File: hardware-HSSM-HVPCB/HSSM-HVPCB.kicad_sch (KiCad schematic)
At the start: 22 parts, among them J1 2086-1103, J2 2601-1110, K1 G6DN-1A-L DC12, K2 G6DN-1A-L DC12, U1 LNK3202D-TL, U2 CS5480-INZ

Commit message: [#3] SCH LNK3204 connections correct output capacitor connection
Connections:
- net +12V: now also C3.1
- net at C1.2, C4.1, D1.1 (K)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: no longer C3.1
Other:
- moved on the sheet: C3, R4
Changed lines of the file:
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@@
 	(paper "A4")
+	(junction
+		(at 240.03 105.41)
+		(diameter 0)
+		(color 0 0 0 0)
+	)
 	(junction
 		(at 224.79 86.36)
@@
 	)
 	(junction
+		(at 251.46 86.36)
+		(diameter 0)
+		(color 0 0 0 0)
+	)
+	(junction
 		(at 240.03 71.12)
 		(diameter 0)
@@
 	)
 	(junction
-		(at 224.79 105.41)
+		(at 160.02 93.98)
 		(diameter 0)
 		(color 0 0 0 0)
 	)
 	(junction
-		(at 240.03 105.41)
-		(diameter 0)
-		(color 0 0 0 0)
-	)
-	(junction
-		(at 160.02 93.98)
+		(at 251.46 105.41)
 		(diameter 0)
 		(color 0 0 0 0)
@@
 	(wire
 		(pts
-			(xy 204.47 105.41) (xy 224.79 105.41)
-		)
-		(stroke
-			(width 0)
-			(type default)
-		)
-	)
-	(wire
-		(pts
-			(xy 240.03 97.79) (xy 240.03 105.41)
+			(xy 204.47 105.41) (xy 240.03 105.41)
+		)
+		(stroke
+			(width 0)
+			(type default)
+		)
+	)
+	(wire
+		(pts
+			(xy 251.46 97.79) (xy 251.46 105.41)
 		)
 		(stroke
@@
 	(wire
 		(pts
-			(xy 224.79 96.52) (xy 224.79 105.41)
-		)
-		(stroke
-			(width 0)
-			(type default)
-		)
-	)
-	(wire
-		(pts
 			(xy 158.75 64.77) (xy 204.47 64.77)
 		)
@@
 	(wire
 		(pts
-			(xy 224.79 86.36) (xy 224.79 91.44)
-		)
-		(stroke
-			(width 0)
-			(type default)
-		)
-	)
-	(wire
-		(pts
 			(xy 133.35 105.41) (xy 133.35 107.95)
 		)
@@
 	(wire
 		(pts
+			(xy 240.03 96.52) (xy 240.03 105.41)
+		)
+		(stroke
+			(width 0)
+			(type default)
+		)
+	)
+	(wire
+		(pts
+			(xy 251.46 86.36) (xy 256.54 86.36)
+		)
+		(stroke
+			(width 0)
+			(type default)
+		)
+	)
+	(wire
+		(pts
 			(xy 139.7 105.41) (xy 133.35 105.41)
 		)
@@
 	(wire
 		(pts
+			(xy 240.03 86.36) (xy 240.03 91.44)
+		)
+		(stroke
+			(width 0)
+			(type default)
+		)
+	)
+	(wire
+		(pts
 			(xy 162.56 68.58) (xy 162.56 82.55)
 		)
@@
 	(wire
 		(pts
-			(xy 240.03 86.36) (xy 256.54 86.36)
-		)
-		(stroke
-			(width 0)
-			(type default)
-		)
-	)
-	(wire
-		(pts
 			(xy 193.04 78.74) (xy 193.04 82.55)
 		)
@@
 	(wire
 		(pts
-			(xy 240.03 105.41) (xy 256.54 105.41)
-		)
-		(stroke
-			(width 0)
-			(type default)
-		)
-	)
-	(wire
-		(pts
 			(xy 224.79 81.28) (xy 224.79 86.36)
 		)
@@
 	(wire
 		(pts
+			(xy 240.03 105.41) (xy 251.46 105.41)
+		)
+		(stroke
+			(width 0)
+			(type default)
+		)
+	)
+	(wire
+		(pts
 			(xy 165.1 86.36) (xy 158.75 86.36)
 		)
@@
 	(wire
 		(pts
-			(xy 240.03 86.36) (xy 240.03 92.71)
+			(xy 251.46 86.36) (xy 251.46 92.71)
+		)
+		(stroke
+			(width 0)
+			(type default)
+		)
+	)
+	(wire
+		(pts
+			(xy 251.46 105.41) (xy 256.54 105.41)
 		)
 		(stroke
@@
 	(wire
 		(pts
+			(xy 240.03 86.36) (xy 251.46 86.36)
+		)
+		(stroke
+			(width 0)
+			(type default)
+		)
+	)
+	(wire
+		(pts
 			(xy 147.32 105.41) (xy 160.02 105.41)
 		)
@@
 		(pts
 			(xy 193.04 73.66) (xy 193.04 68.58)
-		)
-		(stroke
-			(width 0)
-			(type default)
-		)
-	)
-	(wire
-		(pts
-			(xy 224.79 105.41) (xy 240.03 105.41)
 		)
 		(stroke
@@
 	(text "12V DC \n(TODO - set proper voltage with resistors)"
 		(exclude_from_sim no)
-		(at 269.24 94.996 0)
+		(at 264.16 96.774 90)
 		(effects
 			(font
@@
 	(symbol
 		(lib_id "HSSM-HVPCB:R_3k3_5pct_0402_RC0402JR-073K3L")
-		(at 240.03 95.25 90)
+		(at 251.46 95.25 90)
 		(unit 1)
 		(exclude_from_sim no)
@@
 		(fields_autoplaced yes)
 		(property "Reference" "R4"
-			(at 242.57 93.98 90)
+			(at 254 93.98 90)
 			(effects
 				(font
@@
 		)
 		(property "Value" "R_3k3_5pct_0402_RC0402JR-073K3L"
-			(at 247.904 95.25 0)
+			(at 259.334 95.25 0)
 			(effects
 				(font
@@
 		)
 		(property "Footprint" "HSSM-HVPCB:R_0402"
-			(at 250.444 95.25 0)
+			(at 261.874 95.25 0)
 			(effects
 				(font
@@
 		)
 		(property "Datasheet" "https://www.yageo.com/upload/media/product/products/datasheet/rchip/PYu-RC_Group_51_RoHS_L_12.pdf"
-			(at 252.984 95.25 0)
+			(at 264.414 95.25 0)
 			(effects
 				(font
@@
 		)
 		(property "Description" "SMD Resistor, 3.3kΩ, ±5%, 0402, RC0402JR-073K3L"
-			(at 240.03 95.25 0)
+			(at 251.46 95.25 0)
 			(effects
 				(font
@@
 		)
 		(property "MPN" "RC0402JR-073K3L"
-			(at 255.524 95.25 0)
+			(at 266.954 95.25 0)
 			(effects
 				(font
@@
 		)
 		(property "Manufacturer" "Yageo"
-			(at 258.064 95.25 0)
+			(at 269.494 95.25 0)
 			(effects
 				(font
@@
 		)
 		(property "License" "Apache-2.0"
-			(at 260.604 95.25 0)
+			(at 272.034 95.25 0)
 			(effects
 				(font
@@
 		)
 		(property "Author" "Lukasz Nowarkiewicz"
-			(at 263.144 95.25 0)
+			(at 274.574 95.25 0)
 			(effects
 				(font
@@
 		)
 		(property "Val" "3k3"
-			(at 242.57 96.5199 90)
+			(at 254 96.5199 90)
 			(effects
 				(font
@@
 	(symbol
 		(lib_id "HSSM-HVPCB:C_100uF_20pct_16V_5mm_WCAP-ATG5_860020372006")
-		(at 224.79 93.98 270)
+		(at 240.03 93.98 270)
 		(unit 1)
 		(exclude_from_sim no)
@@
 		(fields_autoplaced yes)
 		(property "Reference" "C3"
-			(at 227.33 92.8369 90)
+			(at 242.57 92.8369 90)
 			(effects
 				(font
@@
 		)
 		(property "Value" "C_100uF_20pct_16V_5mm_WCAP-ATG5_860020372006"
+			(at 232.156 93.98 0)
+			(effects
+				(font
+					(size 1.27 1.27)
+					(thickness 0.15)
+				)
+				(justify left bottom)
+				(hide yes)
+			)
+		)
+		(property "Footprint" "HSSM-HVPCB:C_Radial_D5_L11_P2"
+			(at 229.616 93.98 0)
+			(effects
+				(font
+					(size 1.27 1.27)
+					(thickness 0.15)
+				)
+				(justify left bottom)
+				(hide yes)
+			)
+		)
+		(property "Datasheet" "https://www.we-online.com/components/products/datasheet/860020372006.pdf"
+			(at 227.076 93.98 0)
+			(effects
+				(font
+					(size 1.27 1.27)
+					(thickness 0.15)
+				)
+				(justify left bottom)
+				(hide yes)
+			)
+		)
+		(property "Description" "Aluminum Electrolytic Capacitor, 100 µF, 16V, ±20%, Radial Leaded, 5mm Diameter, WCAP-ATG5 Series"
+			(at 240.03 93.98 0)
+			(effects
+				(font
+					(size 1.27 1.27)
+				)
+				(hide yes)
+			)
+		)
+		(property "MPN" "860020372006"
+			(at 224.536 93.98 0)
+			(effects
+				(font
+					(size 1.27 1.27)
+					(thickness 0.15)
+				)
+				(justify left bottom)
+				(hide yes)
+			)
+		)
+		(property "Manufacturer" "Würth Elektronik"
+			(at 221.996 93.98 0)
+			(effects
+				(font
+					(size 1.27 1.27)
+					(thickness 0.15)
+				)
+				(justify left bottom)
+				(hide yes)
+			)
+		)
+		(property "License" "Apache-2.0"
+			(at 219.456 93.98 0)
+			(effects
+				(font
+					(size 1.27 1.27)
+				)
+				(justify left bottom)
+				(hide yes)
+			)
+		)
+		(property "Author" "Lukasz Nowarkiewicz"
 			(at 216.916 93.98 0)
 			(effects
 				(font
 					(size 1.27 1.27)
-					(thickness 0.15)
-				)
-				(justify left bottom)
-				(hide yes)
-			)
-		)
-		(property "Footprint" "HSSM-HVPCB:C_Radial_D5_L11_P2"
-			(at 214.376 93.98 0)
-			(effects
-				(font
-					(size 1.27 1.27)
-					(thickness 0.15)
-				)
-				(justify left bottom)
-				(hide yes)
-			)
-		)
-		(property "Datasheet" "https://www.we-online.com/components/products/datasheet/860020372006.pdf"
-			(at 211.836 93.98 0)
-			(effects
-				(font
-					(size 1.27 1.27)
-					(thickness 0.15)
-				)
-				(justify left bottom)
-				(hide yes)
-			)
-		)
-		(property "Description" "Aluminum Electrolytic Capacitor, 100 µF, 16V, ±20%, Radial Leaded, 5mm Diameter, WCAP-ATG5 Series"
-			(at 224.79 93.98 0)
-			(effects
-				(font
-					(size 1.27 1.27)
-				)
-				(hide yes)
-			)
-		)
-		(property "MPN" "860020372006"
-			(at 209.296 93.98 0)
-			(effects
-				(font
-					(size 1.27 1.27)
-					(thickness 0.15)
-				)
-				(justify left bottom)
-				(hide yes)
-			)
-		)
-		(property "Manufacturer" "Würth Elektronik"
-			(at 206.756 93.98 0)
-			(effects
-				(font
-					(size 1.27 1.27)
-					(thickness 0.15)
-				)
-				(justify left bottom)
-				(hide yes)
-			)
-		)
-		(property "License" "Apache-2.0"
-			(at 204.216 93.98 0)
-			(effects
-				(font
-					(size 1.27 1.27)
-				)
-				(justify left bottom)
-				(hide yes)
-			)
-		)
-		(property "Author" "Lukasz Nowarkiewicz"
-			(at 201.676 93.98 0)
-			(effects
-				(font
-					(size 1.27 1.27)
 				)
 				(justify left bottom)
@@
 		)
 		(property "Val" "100µF"
-			(at 227.33 95.3768 90)
-			(effects
-				(font
+			(at 242.57 95.3768 90)
+			(effects
+				(font

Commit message: [#3] Correct MURS160-E3/52T
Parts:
- D1: Val D_rect_1A_600V_SOD123FL_MURS160-E3_52T -> 1A_600V
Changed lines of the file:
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@@
 			)
 		)
-		(property "Val" "D_rect_1A_600V_SOD123FL_MURS160-E3_52T"
-			(at 208.026 97.282 0)
+		(property "Val" "1A_600V"
+			(at 207.01 96.266 90)
 			(effects
 				(font

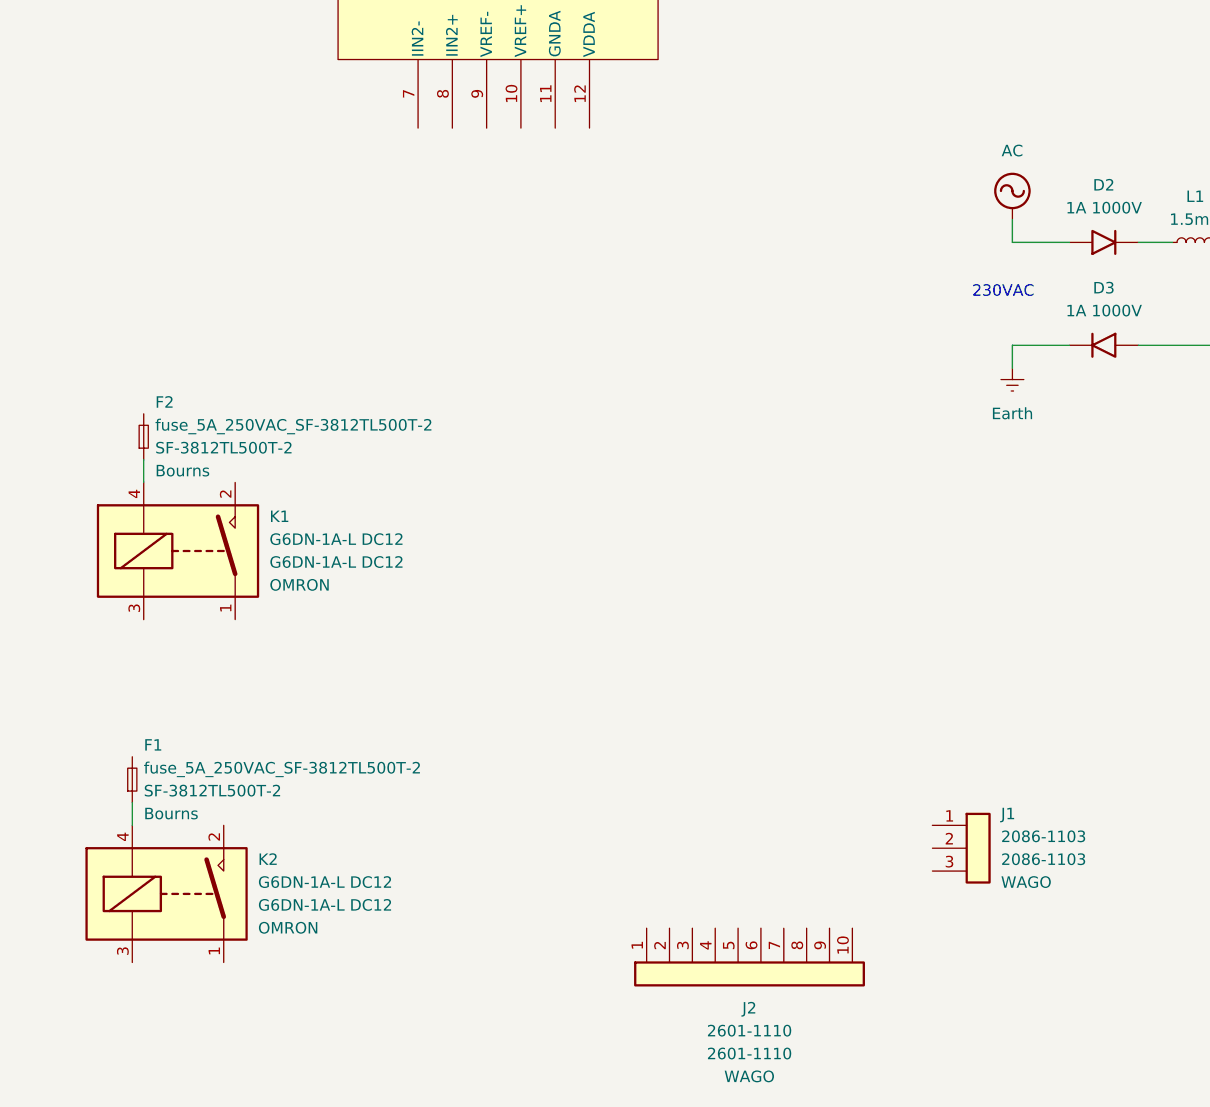
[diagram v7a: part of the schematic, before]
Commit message: [#3] SCH add relay control
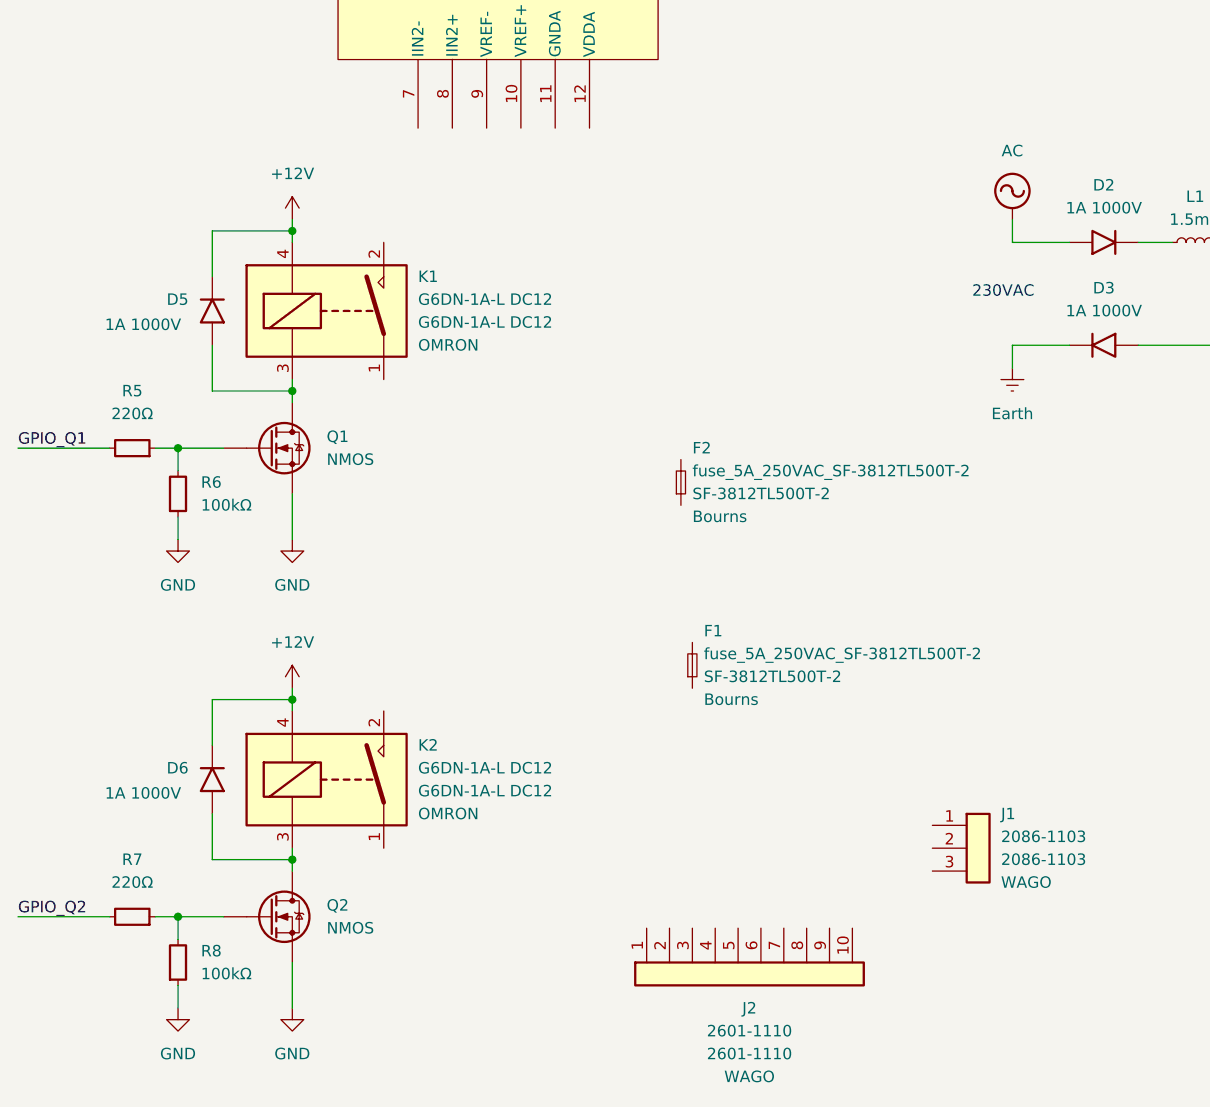
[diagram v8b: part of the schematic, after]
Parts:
- added D5, D6: D_rect_1A_1000V_SOD123_1N4007W, HSSM-HVPCB:D_SOD123, symbol HSSM-HVPCB:D_rect_1A_1000V_SOD123_1N4007W
- added Q1, Q2: Q_NMOS_SOT-23_IRLML6344, HSSM-HVPCB:Q_SOT23, symbol HSSM-HVPCB:Q_NMOS_SOT-23_IRLML6344
- added R5, R7: R_220R_1pct_0402_RC0402FR-07220RL, HSSM-HVPCB:R_0402, symbol HSSM-HVPCB:R_220R_1pct_0402_RC0402FR-07220RL
- added R6, R8: R_100k_1pct_0402_RC0402FR-07100KL, HSSM-HVPCB:R_0402, symbol HSSM-HVPCB:R_100k_1pct_0402_RC0402FR-07100KL
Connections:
- net +12V: now also K1.4, K2.4, D5.1 (K), D6.1 (K)
- net GND: now also Q1.3 (S), Q2.3 (S), R6.1, R8.1
- net at K1.3: now also D5.2 (A), Q1.1 (D)
- net at F2.1: no longer K1.4
- net at K2.3: now also D6.2 (A), Q2.1 (D)
- net at F1.1: no longer K2.4
- new net: Q1.2 (G), R5.1, R6.2
- new net: Q2.2 (G), R7.1, R8.2
- new net GPIO_Q1: R5.2
- new net GPIO_Q2: R7.2
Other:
- moved on the sheet: F1, F2, K1
